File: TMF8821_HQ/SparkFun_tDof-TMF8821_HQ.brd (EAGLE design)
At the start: 25.4 x 12.7 mm, 48 parts, among them J4 QWIIC_RIGHT_ANGLE, J5 QWIIC_RIGHT_ANGLE

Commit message: Adds default address to HQ boards, fixes some clearance issues
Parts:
- moved R1 0.18 mm to (46.5, 32.1)
- moved C2 0.13 mm to (44.1, 32.1)

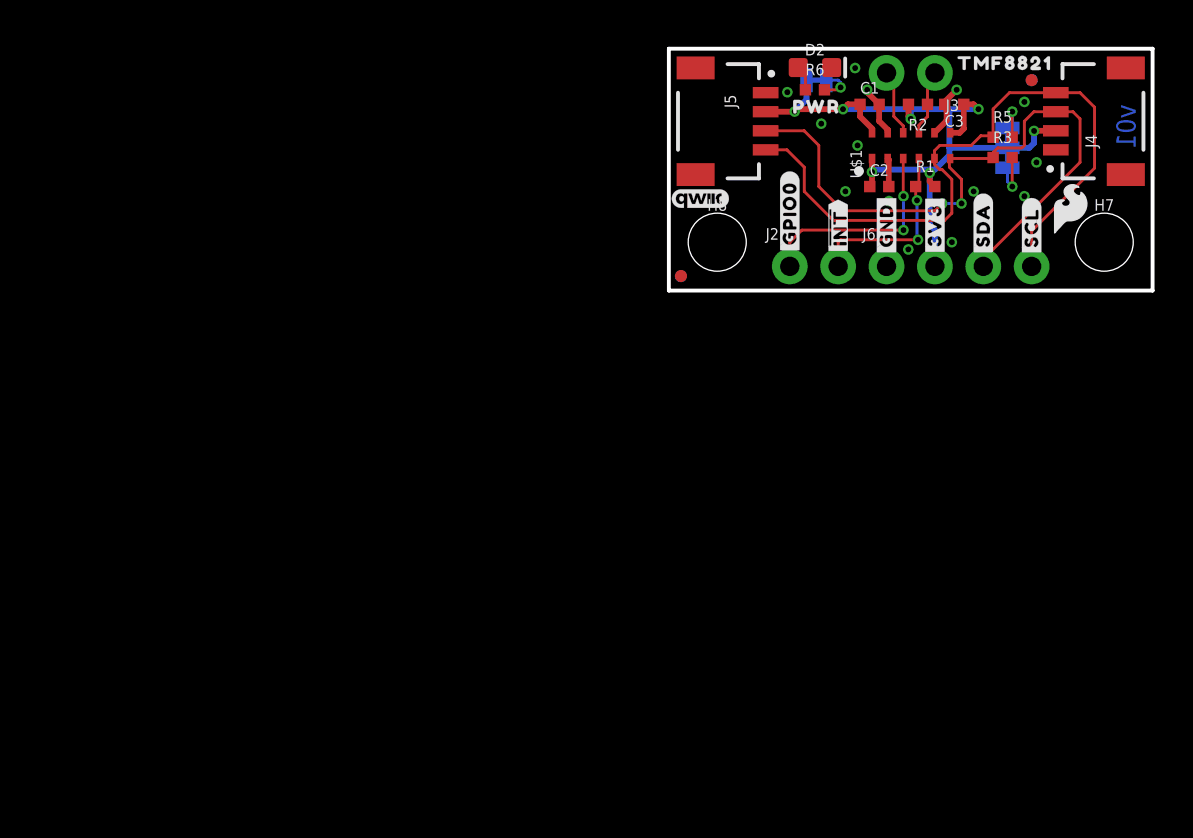
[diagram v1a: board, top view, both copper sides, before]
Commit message: Copies 8820 designs to create 8821 designs - updates relevant references to 8820 to 8821
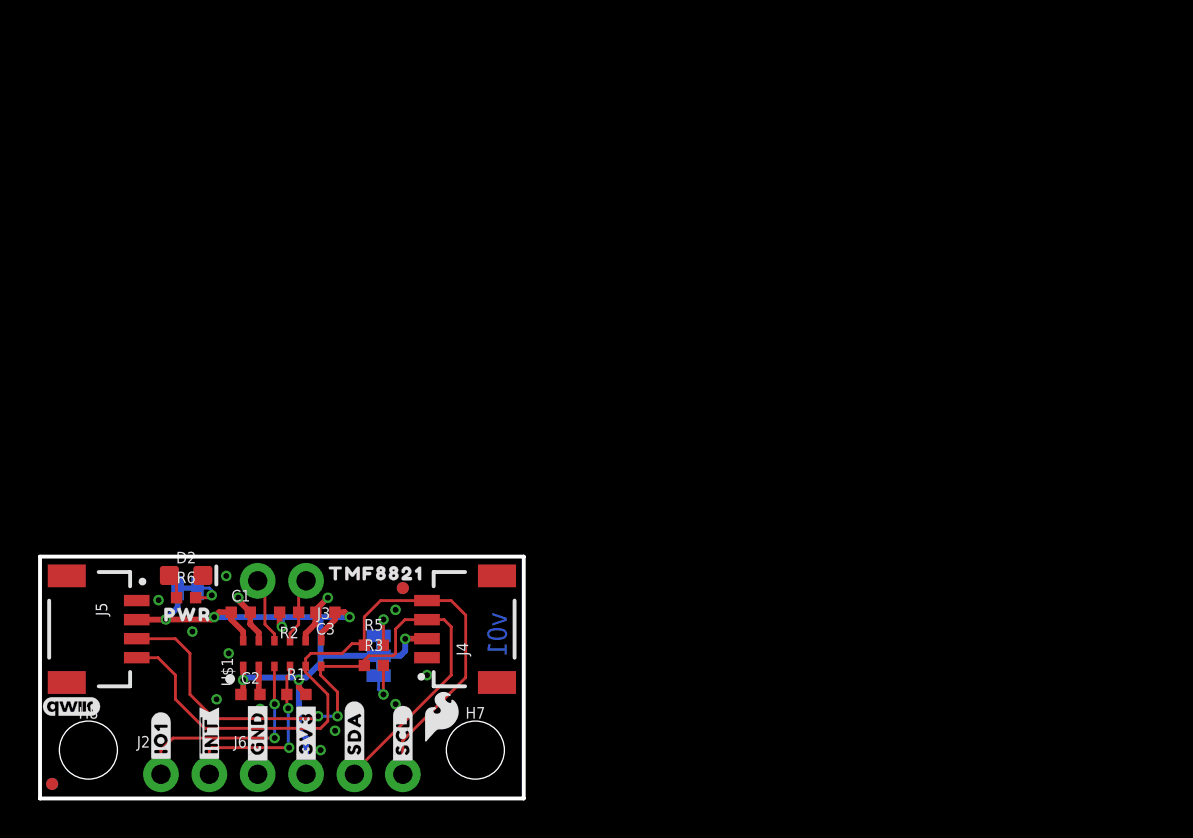
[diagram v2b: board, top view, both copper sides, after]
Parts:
- removed U$17: (no value), TMFHQBotSilk:#GPIO1#8
- removed U$21: (no value), TMFHQTopSilk:##INT##20
- removed U$23: (no value), TMFHQBotSilk:#SYNC#8
- removed U$32: (no value), TMFHQTopSilk:DTOF8821882023
- removed U$41: (no value), TMFHQBotSilk:##INT##9
- removed U$42: (no value), TMFHQTopSilk:#GPIO0#19
- added U$4: (no value), TMFHQTopSilk:##INT##8
- added U$5: (no value), TMFHQBotSilk:#SYNC#8
- added U$6: (no value), TMFHQTopSilk:#IO1#8
- added U$7: (no value), TMFHQTopSilk:DTOF882188211
- added U$8: (no value), TMFHQTopSilk:TMF882188210
- added U$9: (no value), TMFHQBotSilk:TMF882113
- U$1: value TMF8821- -> TMF882X_TMF8821
- U$2: device TMFHQTopSilk:TMF8821882021 -> TMFHQBotSilk:#IO1#8
- U$3: device TMFHQTopSilk:TMF8821882021 -> TMFHQBotSilk:##INT##9
- moved U$2 56.7 mm to (6.35, 3.17), turned to 90 degrees
- moved C2 42.4 mm to (11.0, 5.46)
- moved D2 42.4 mm to (7.67, 11.7)
- moved FD5 42.4 mm to (19.1, 11.0)
- moved FD6 42.4 mm to (0.64, 0.76)
- moved FD7 42.4 mm to (0.64, 0.76)
- moved FD8 42.4 mm to (19.1, 11.0)
- moved H7 42.4 mm to (22.9, 2.54)
- moved H8 42.4 mm to (2.54, 2.54)
- moved J2 42.4 mm to (6.35, 1.27)
- moved J3 42.4 mm to (14.0, 11.4)
- moved J4 42.4 mm to (20.3, 8.89)
- moved J5 42.4 mm to (5.08, 8.89)
- moved J6 42.4 mm to (11.4, 1.27)
- moved LED 42.4 mm to (7.75, 11.0)
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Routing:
- net SDA: track 34.8 -> 35.3 mm
- net GND: track 7.02 -> 6.61 mm, vias 14 -> 13
